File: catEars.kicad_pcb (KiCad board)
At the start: 2 copper layers, 41.3 x 41.4 mm, 26 parts, among them J1 Conn_01x03_Socket, J2 Conn_01x03_Socket, U1 ESP-01v090, U2 AMS1117-3.3

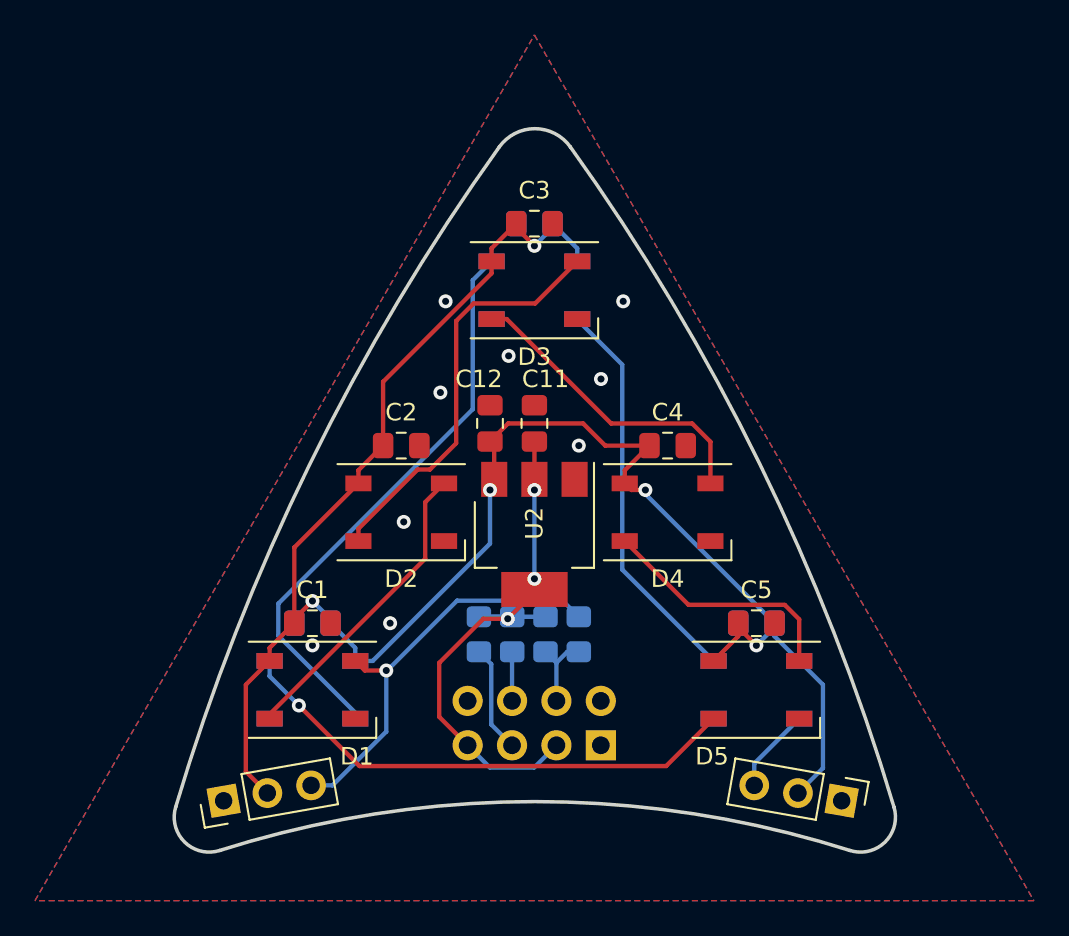
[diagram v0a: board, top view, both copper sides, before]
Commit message: new positioning for components
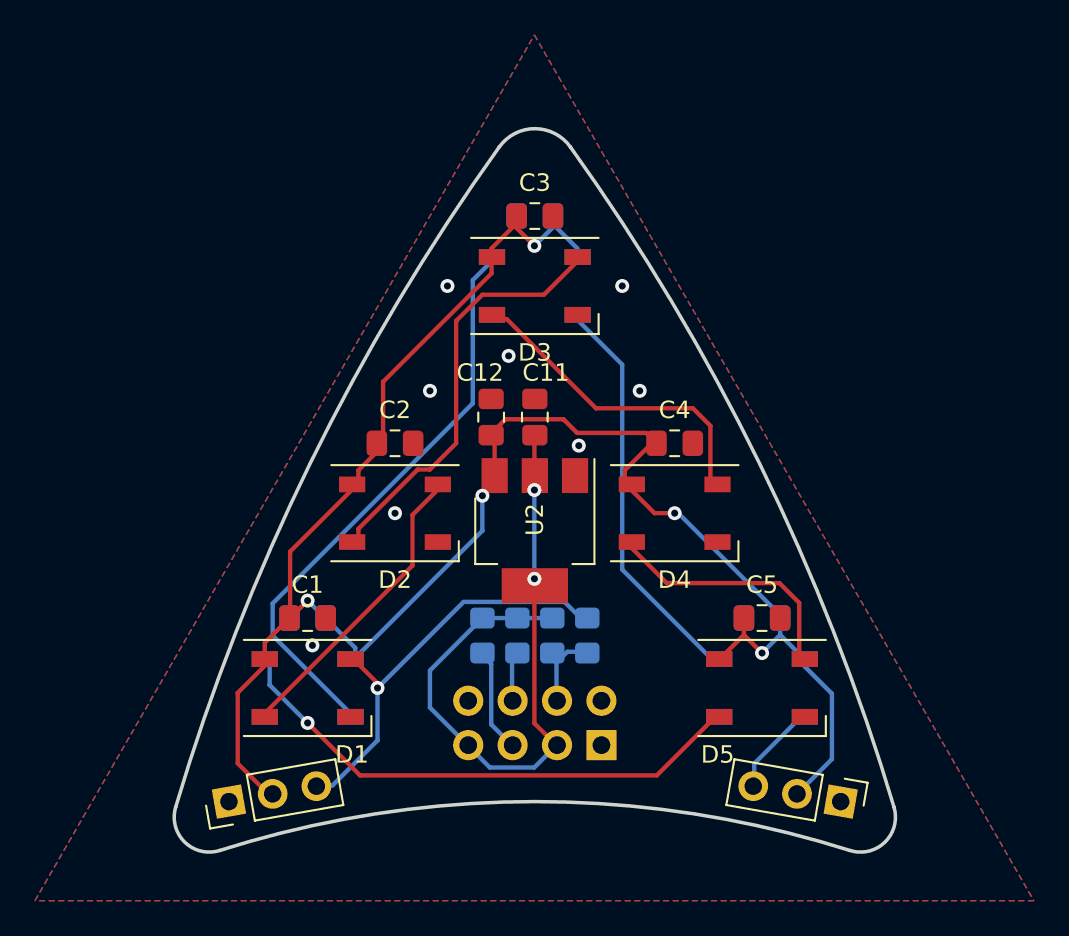
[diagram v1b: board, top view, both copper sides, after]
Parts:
- moved R4 0.49 mm to (3.00, 29.0)
- moved C5 0.44 mm to (13.0, 28.0)
- moved C8 0.44 mm to (13.0, 28.0)
- moved C3 0.43 mm to (0.00, 5.00)
- moved C7 0.43 mm to (0.00, 5.00)
- moved C4 0.43 mm to (8.00, 18.0)
- moved D4 0.41 mm to (8.00, 22.0)
- moved C1 0.40 mm to (-13.0, 28.0)
- moved C6 0.40 mm to (-13.0, 28.0)
- moved R3 0.40 mm to (1.00, 29.0)
- moved C2 0.38 mm to (-8.00, 18.0)
- moved C12 0.37 mm to (-2.50, 16.5)
- moved C11 0.36 mm to (0.00, 16.5)
- moved D2 0.36 mm to (-8.00, 22.0)
- moved D5 0.34 mm to (13.0, 32.0)
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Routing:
- net 3V3: track 31.8 -> 37.1 mm, vias 3 -> 2
- net +5V: track 110.1 -> 110.9 mm
- net Net-(D5-DOUT): track 29.5 -> 30.3 mm
- net Net-(D4-DOUT): track 14.2 -> 14.8 mm
- net Net-(D3-DOUT): track 17.8 -> 18.3 mm
- net GND: vias 9 -> 8

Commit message: added 2 leds and smd ESP Socket to PCB
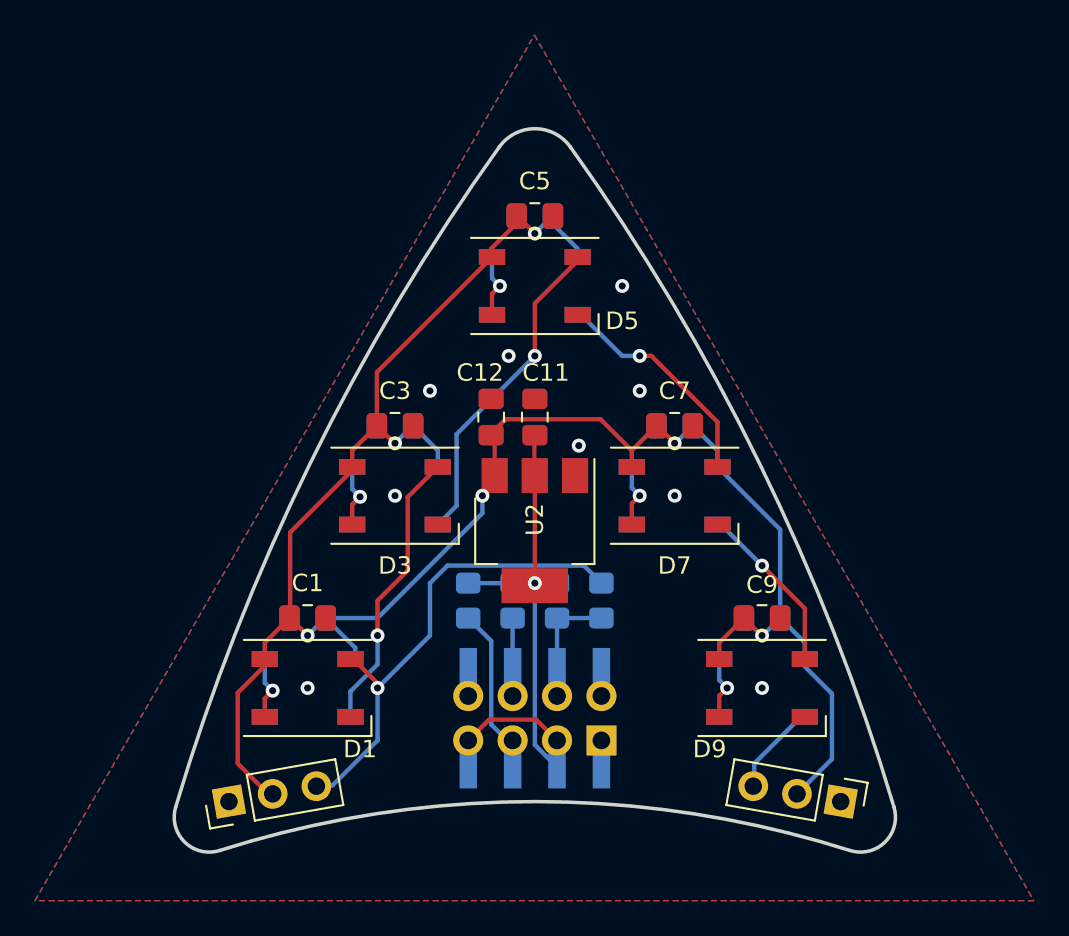
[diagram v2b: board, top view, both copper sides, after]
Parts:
- added C4: 100nF, Capacitor_SMD:C_0805_2012Metric_Pad1.18x1.45mm_HandSolder, B.Cu at (-8.00, 17.0)
- added C8: 100nF, Capacitor_SMD:C_0805_2012Metric_Pad1.18x1.45mm_HandSolder, B.Cu at (8.00, 17.0)
- added D4: WS2812B, LED_SMD:LED_WS2812B_PLCC4_5.0x5.0mm_P3.2mm, B.Cu at (-8.00, 21.0)
- added D8: WS2812B, LED_SMD:LED_WS2812B_PLCC4_5.0x5.0mm_P3.2mm, B.Cu at (8.00, 21.0)
- added U1_: PinSocket_2x04_P2.54mm_Vertical_SMD, Connector_PinSocket_2.54mm:PinSocket_2x04_P2.54mm_Vertical_SMD, B.Cu at (0.00, 33.7)
- C12: value 10uF -> 22uF
- moved R1 2.16 mm to (-3.81, 27.0)
- moved R4 2.16 mm to (3.81, 27.0)
- moved R2 2.02 mm to (-1.27, 27.0)
- moved R3 2.02 mm to (1.27, 27.0)
- moved C3 1.00 mm to (-8.00, 17.0)
- moved C7 1.00 mm to (8.00, 17.0)
- moved D3 1.00 mm to (-8.00, 21.0)
- moved D7 1.00 mm to (8.00, 21.0)
- moved U1 0.27 mm to (3.81, 35.0)
- renumbered C8 to C10, C6 to C2, C2 to C3, C3 to C5, C7 to C6, C4 to C7, C5 to C9, D8 to D10, D6 to D2, D2 to D3, D3 to D5, D7 to D6, D4 to D7, D5 to D9
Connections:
- D10 pad 4: Net-(D7-DOUT) -> Net-(D10-DIN)
- D2 pad 2: Net-(D6-DOUT) -> Net-(D2-DOUT)
- D2 pad 4: Net-(D5-DOUT) -> Net-(D1-DOUT)
- D3 pad 2: Net-(D2-DOUT) -> Net-(D3-DOUT)
- D3 pad 4: Net-(D1-DOUT) -> Net-(D2-DOUT)
- D5 pad 2: Net-(D3-DOUT) -> Net-(D5-DOUT)
- D5 pad 4: Net-(D2-DOUT) -> Net-(D4-DOUT)
- D6 pad 2: Net-(D7-DOUT) -> Net-(D6-DOUT)
- D6 pad 4: Net-(D6-DOUT) -> Net-(D5-DOUT)
- D7 pad 2: Net-(D4-DOUT) -> Net-(D7-DOUT)
- D7 pad 4: Net-(D3-DOUT) -> Net-(D6-DOUT)
- D9 pad 2: Net-(D5-DOUT) -> Net-(D10-DIN)
- D9 pad 4: Net-(D4-DOUT) -> Net-(D8-DOUT)
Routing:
- net Net-(D5-DOUT): track 30.3 -> 3.67 mm
- net Net-(D6-DOUT): track 33.3 -> 13.1 mm, vias 0 -> 1
- net Net-(D7-DOUT): track 22.8 -> 3.67 mm, vias 0 -> 1
- net Net-(D3-DOUT): track 18.3 -> 3.87 mm, vias 0 -> 1
- net Net-(D1-DOUT): track 17.9 -> 4.12 mm, vias 0 -> 1
- net Net-(D8-DOUT): track 0.00 -> 9.89 mm, vias 0 -> 1
- net +5V: track 110.9 -> 119.3 mm, vias 5 -> 6
- net Net-(D2-DOUT): track 23.7 -> 16.4 mm, vias 0 -> 1
- net 3V3: track 37.1 -> 30.8 mm, vias 2 -> 1
- net LED: track 23.9 -> 27.8 mm
- net Net-(D4-DOUT): track 14.8 -> 18.6 mm, vias 0 -> 1
- net Net-(D10-DIN): track 0.00 -> 3.67 mm, vias 0 -> 1
- net Net-(U1-RST): track 6.13 -> 8.32 mm
- net Net-(U1-GPIO2): track 4.61 -> 5.75 mm
- net Net-(U1-GPIO0): track 2.81 -> 3.48 mm
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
